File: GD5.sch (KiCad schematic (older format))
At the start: 19 parts, among them IC7 HCPL-316J, IC8 IXDD614PI, P4 CONN_01X03, P5 CONN_01X03

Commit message: uding HCPL-361J modified symbol
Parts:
- IC7: symbol HCPL-316J-RESCUE-gatedrive -> HCPL-316J
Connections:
- wire segments 41 -> 50
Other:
- moved on the sheet: IC8
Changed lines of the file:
@@
 EESchema Schematic File Version 2
-LIBS:gatedrive-rescue
 LIBS:power
 LIBS:device
@@
 LIBS:contrib
 LIBS:valves
-LIBS:GateDrive
+LIBS:74xgxx
+LIBS:ac-dc
+LIBS:actel
+LIBS:Altera
+LIBS:analog_devices
+LIBS:brooktre
+LIBS:cmos_ieee
+LIBS:dc-dc
+LIBS:diode
+LIBS:elec-unifil
+LIBS:ESD_Protection
+LIBS:ftdi
+LIBS:gennum
+LIBS:graphic
+LIBS:hc11
+LIBS:ir
+LIBS:Lattice
+LIBS:logo
+LIBS:maxim
+LIBS:microchip_dspic33dsc
+LIBS:microchip_pic10mcu
+LIBS:microchip_pic12mcu
+LIBS:microchip_pic16mcu
+LIBS:microchip_pic18mcu
+LIBS:microchip_pic32mcu
+LIBS:motor_drivers
+LIBS:msp430
+LIBS:nordicsemi
+LIBS:nxp_armmcu
+LIBS:onsemi
+LIBS:Oscillators
+LIBS:powerint
+LIBS:Power_Management
+LIBS:pspice
+LIBS:references
+LIBS:relays
+LIBS:rfcom
+LIBS:sensors
+LIBS:silabs
+LIBS:stm8
+LIBS:stm32
+LIBS:supertex
+LIBS:switches
+LIBS:transf
+LIBS:ttl_ieee
+LIBS:video
+LIBS:Worldsemi
+LIBS:Xicor
+LIBS:Zilog
 LIBS:gatedrive-cache
 EELAYER 25 0
@@
 L IXDD614PI-RESCUE-gatedrive IC8
 U 1 1 56EF642F
-P 7900 5100
-F 0 "IC8" H 7900 4900 60  0000 C CNN
-F 1 "IXDD614PI" H 7950 5450 60  0000 C CNN
-F 2 "gatedrive:DIP-8_W7.62mm_LongPads" H 7900 5200 60  0001 C CNN
-F 3 "" H 7900 5200 60  0000 C CNN
-F 4 "CHINA[already bought]" H 7900 5100 60  0001 C CNN "Supplier"
-	1    7900 5100
-	1    0    0    -1
-$EndComp
-$Comp
-L HCPL-316J-RESCUE-gatedrive IC7
+P 7950 5100
+AR Path="/56EF642F" Ref="IC8"  Part="1"
+AR Path="/56EF0563/56EF642F" Ref="IC8"  Part="1"
+F 0 "IC8" H 7950 4900 60  0000 C CNN
+F 1 "IXDD614PI" H 8000 5450 60  0000 C CNN
+F 2 "gatedrive:DIP-8_W7.62mm_LongPads" H 7950 5200 60  0001 C CNN
+F 3 "" H 7950 5200 60  0000 C CNN
+F 4 "CHINA[already bought]" H 7950 5100 60  0001 C CNN "Supplier"
+	1    7950 5100
+	1    0    0    -1
+$EndComp
+$Comp
+L HCPL-316J IC7
 U 1 1 56EF6430
-P 5550 4750
-F 0 "IC7" H 5550 4150 60  0000 C CNN
-F 1 "HCPL-316J" H 5300 5200 60  0000 C CNN
-F 2 "Housings_SOIC:SOIC-16_7.5x10.3mm_Pitch1.27mm" H 5550 4750 60  0001 C CNN
-F 3 "" H 5550 4750 60  0000 C CNN
-F 4 "CHINA [ already bought]" H 5550 4750 60  0001 C CNN "Supplier"
-	1    5550 4750
+P 5600 4850
+F 0 "IC7" H 5600 4250 60  0000 C CNN
+F 1 "HCPL-316J" H 5350 5300 60  0000 C CNN
+F 2 "Housings_SOIC:SOIC-16_7.5x10.3mm_Pitch1.27mm" H 5600 4850 60  0001 C CNN
+F 3 "" H 5600 4850 60  0000 C CNN
+F 4 "CHINA [ already bought]" H 5600 4850 60  0001 C CNN "Supplier"
+	1    5600 4850
 	1    0    0    -1
 $EndComp
@@
 Text GLabel 6450 4800 2    60   Input ~ 0
 15V5
-Text GLabel 7500 4850 0    60   Input ~ 0
-15V5
-Text GLabel 7500 5150 0    60   Input ~ 0
--5V5
-Text GLabel 8350 5150 2    60   Input ~ 0
+Text GLabel 7550 4850 0    60   Input ~ 0
+15V5
+Text GLabel 7550 5150 0    60   Input ~ 0
+-5V5
+Text GLabel 8300 5150 2    60   Input ~ 0
 -5V5
 Text GLabel 10200 4950 2    60   Input ~ 0
@@
 a cap to ensure soft turn-off, recommended by datasheet of hcpl.
 Wire Wire Line
-	6950 4950 7500 4950
-Wire Wire Line
-	6250 4950 6650 4950
-Wire Wire Line
-	6250 5050 6250 5150
-Wire Wire Line
-	6250 4750 6250 4850
+	6950 4950 7150 4950
+Wire Wire Line
+	7150 4950 7550 4950
+Wire Wire Line
+	5800 4950 6500 4950
+Wire Wire Line
+	6500 4950 6650 4950
+Wire Wire Line
+	5800 5050 6250 5100
+Wire Wire Line
+	6250 5100 5800 5150
+Wire Wire Line
+	5800 4750 6250 4800
+Wire Wire Line
+	6250 4800 5800 4850
 Connection ~ 6550 4100
 Wire Wire Line
-	6550 4650 6250 4650
+	6550 4650 5800 4650
 Wire Wire Line
 	6550 4100 6650 4100
 Wire Wire Line
-	6550 4050 6550 4650
+	6550 4050 6550 4100
+Wire Wire Line
+	6550 4100 6550 4650
 Connection ~ 8450 4950
 Wire Wire Line
@@
 Connection ~ 7150 4950
 Wire Wire Line
-	3625 4650 4850 4650
-Wire Wire Line
-	8350 4950 9050 4950
+	3625 4650 4000 4650
+Wire Wire Line
+	4000 4650 4900 4650
+Wire Wire Line
+	8300 4950 8450 4950
+Wire Wire Line
+	8450 4950 8900 4950
+Wire Wire Line
+	8900 4950 9050 4950
 Wire Wire Line
 	9350 4950 9450 4950
 Wire Wire Line
-	9750 4950 10200 4950
+	9750 4950 9950 4950
+Wire Wire Line
+	9950 4950 10200 4950
 Wire Wire Line
 	9750 5250 9950 5250
@@
 Connection ~ 9950 4950
 Wire Wire Line
-	8350 5050 8450 5050
+	8300 5050 8450 5050
 Wire Wire Line
 	8450 5050 8450 4950
@@
 	4400 4350 4400 4550
 Wire Wire Line
-	4400 4550 4850 4550
+	4400 4550 4900 4550
 Wire Wire Line
 	4000 4350 4000 4650
@@
 	4000 5300 4000 4750
 Wire Wire Line
-	4000 4750 4850 4750
-Wire Wire Line
-	4850 5150 4750 5150
+	4000 4750 4900 4750
+Wire Wire Line
+	4900 5150 4750 5150
 Wire Wire Line
 	4750 5150 4750 5300
 Wire Wire Line
-	4850 4850 4400 4850
+	4900 4850 4400 4850
 Wire Wire Line
 	4400 4850 4400 5300
 Wire Wire Line
-	6250 4450 6300 4450
+	5800 4450 6300 4450
 Wire Wire Line
 	6300 4450 6300 4350
@@
 Wire Wire Line
 	6500 5000 6500 4950
-Text GLabel 8350 4850 2    60   Input ~ 0
+Text GLabel 8300 4850 2    60   Input ~ 0
 15V5
 Text GLabel 7175 5075 3    60   Input ~ 0
 15V5
 Wire Wire Line
-	7500 5050 7175 5050
+	7550 5050 7175 5050
 Wire Wire Line
 	7175 5050 7175 5075
-Text GLabel 4850 4950 0    60   Input ~ 0
+Text GLabel 4900 4950 0    60   Input ~ 0
 ~FAULT
 Text GLabel 4750 5300 3    60   Input ~ 0
@@
 Text GLabel 1475 3050 0    60   Input ~ 0
 ~RST
-Text HLabel 4850 4450 0    60   Input ~ 0
+Text HLabel 4900 4450 0    60   Input ~ 0
 T5
 $Comp

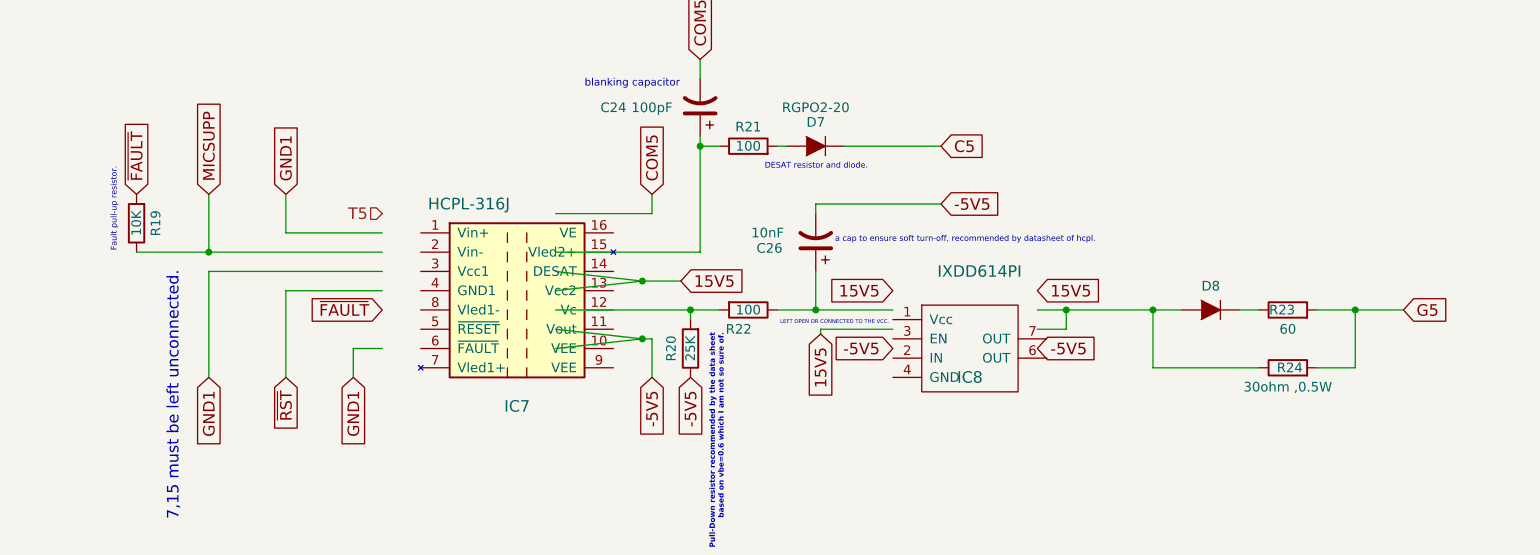
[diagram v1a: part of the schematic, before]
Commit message: cleaning the schematic
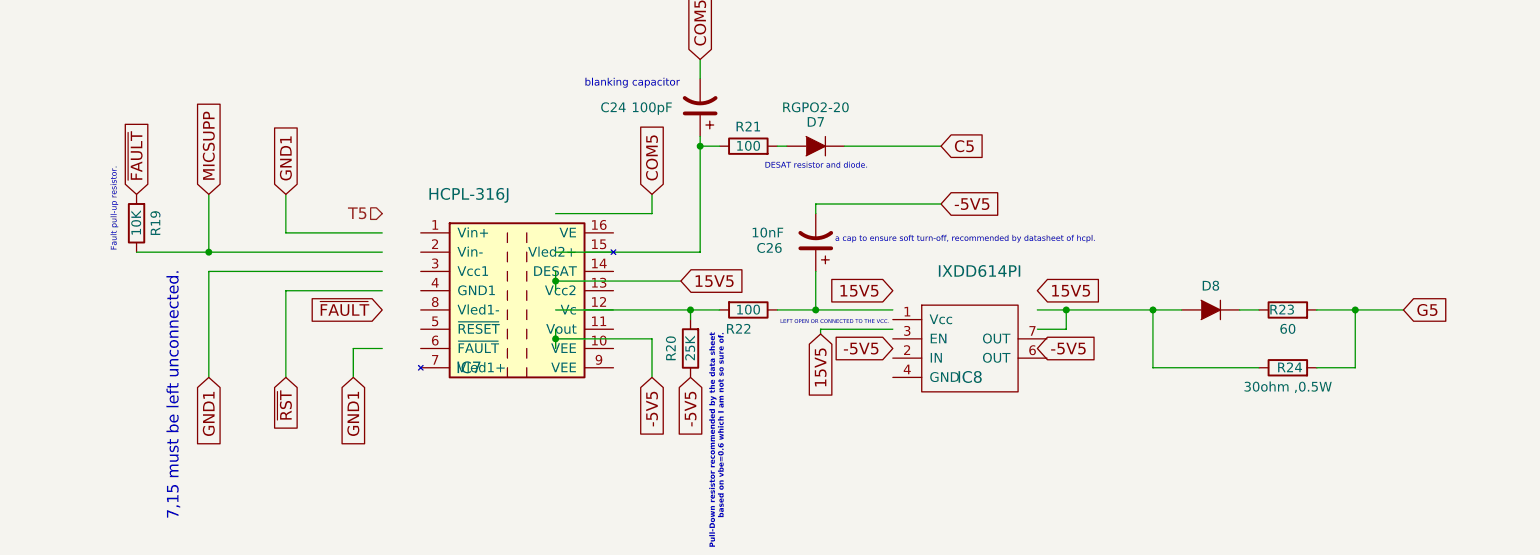
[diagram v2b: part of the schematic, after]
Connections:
- wire segments 50 -> 41
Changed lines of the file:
@@
 U 1 1 56EF6430
 P 5600 4850
-F 0 "IC7" H 5600 4250 60  0000 C CNN
-F 1 "HCPL-316J" H 5350 5300 60  0000 C CNN
+F 0 "IC7" H 5350 4450 60  0000 C CNN
+F 1 "HCPL-316J" H 5350 5350 60  0000 C CNN
 F 2 "Housings_SOIC:SOIC-16_7.5x10.3mm_Pitch1.27mm" H 5600 4850 60  0001 C CNN
 F 3 "" H 5600 4850 60  0000 C CNN
@@
 a cap to ensure soft turn-off, recommended by datasheet of hcpl.
 Wire Wire Line
-	6950 4950 7150 4950
-Wire Wire Line
-	7150 4950 7550 4950
-Wire Wire Line
-	5800 4950 6500 4950
-Wire Wire Line
-	6500 4950 6650 4950
-Wire Wire Line
-	5800 5050 6250 5100
-Wire Wire Line
-	6250 5100 5800 5150
-Wire Wire Line
-	5800 4750 6250 4800
-Wire Wire Line
-	6250 4800 5800 4850
+	6950 4950 7550 4950
+Wire Wire Line
+	5800 4950 6650 4950
+Wire Wire Line
+	5800 5050 5800 5150
+Wire Wire Line
+	5800 4750 5800 4850
 Connection ~ 6550 4100
 Wire Wire Line
@@
 	6550 4100 6650 4100
 Wire Wire Line
-	6550 4050 6550 4100
-Wire Wire Line
-	6550 4100 6550 4650
+	6550 4050 6550 4650
 Connection ~ 8450 4950
 Wire Wire Line
@@
 Connection ~ 7150 4950
 Wire Wire Line
-	3625 4650 4000 4650
-Wire Wire Line
-	4000 4650 4900 4650
-Wire Wire Line
-	8300 4950 8450 4950
-Wire Wire Line
-	8450 4950 8900 4950
-Wire Wire Line
-	8900 4950 9050 4950
+	3625 4650 4900 4650
+Wire Wire Line
+	8300 4950 9050 4950
 Wire Wire Line
 	9350 4950 9450 4950
 Wire Wire Line
-	9750 4950 9950 4950
-Wire Wire Line
-	9950 4950 10200 4950
+	9750 4950 10200 4950
 Wire Wire Line
 	9750 5250 9950 5250
@@
 	6300 5300 6300 5100
 Wire Wire Line
-	6300 5100 6250 5100
-Connection ~ 6250 5100
-Wire Wire Line
-	6250 4800 6450 4800
-Connection ~ 6250 4800
+	6300 5100 5800 5100
+Connection ~ 5800 5100
+Wire Wire Line
+	5800 4800 6450 4800
+Connection ~ 5800 4800
 Wire Wire Line
 	8900 5250 9450 5250

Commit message: completion of the layout, initial layout of the protection circuit, reducing number of circuit to 7
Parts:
- C22, C23, C24, C26, C27, C28: footprint Capacitors_ThroughHole:C_Disc_D3_P2.5 -> gatedrive:C_Disc
- D7: footprint Diodes_ThroughHole:Diode_DO-201AD_Horizontal_RM15 -> Diodes_ThroughHole:Diode_DO-41_SOD81_Horizontal_RM10
- R19: footprint Resistors_ThroughHole:Resistor_Vertical_RM5mm -> Resistors_ThroughHole:Resistor_Horizontal_RM10mm
- R23, R24: footprint Resistors_ThroughHole:Resistor_Horizontal_RM20mm -> gatedrive:Resistor_multi
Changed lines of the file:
@@
 EESchema Schematic File Version 2
+LIBS:Symbols_DCDC-ACDC-Converter_RevC_20Jul2012
+LIBS:Symbols_EN60617_13Mar2013
+LIBS:Symbols_EN60617-10_HF-Radio_DRAFT_12Sep2013
+LIBS:Symbols_ICs-Diskrete_RevD10
+LIBS:Symbols_ICs-Opto_RevB_16Sep2013
+LIBS:Symbols_Microcontroller_Philips-NXP_RevA_06Oct2013
+LIBS:SymbolsSimilarEN60617+oldDIN617-RevE8
+LIBS:Symbols_Socket-DIN41612_RevA
+LIBS:Symbols_Transformer-Diskrete_RevA
 LIBS:power
 LIBS:device
@@
 $Descr A4 11693 8268
 encoding utf-8
-Sheet 5 10
+Sheet 5 9
 Title "IGBT GATE DRIVE SCHEMATIC."
 Date "2016-03-02"
@@
 F 0 "D7" H 7150 3976 50  0000 C CNN
 F 1 "RGPO2-20" H 7150 3900 50  0000 C CNN
-F 2 "Diodes_ThroughHole:Diode_DO-201AD_Horizontal_RM15" H 7150 4100 50  0001 C CNN
+F 2 "Diodes_ThroughHole:Diode_DO-41_SOD81_Horizontal_RM10" H 7150 4100 50  0001 C CNN
 F 3 "" H 7150 4100 50  0000 C CNN
 F 4 "El-Amir" H 7150 4100 60  0001 C CNN "Supplier"
@@
 F 0 "R19" V 3525 4500 50  0000 C CNN
 F 1 "10K" V 3625 4500 50  0000 C CNN
-F 2 "Resistors_ThroughHole:Resistor_Vertical_RM5mm" V 3555 4500 50  0001 C CNN
+F 2 "Resistors_ThroughHole:Resistor_Horizontal_RM10mm" V 3555 4500 50  0001 C CNN
 F 3 "" H 3625 4500 50  0000 C CNN
 F 4 "EL AMIR" H 3625 4500 60  0001 C CNN "Supplier"
@@
 F 0 "C22" H 4150 2150 50  0000 C CNN
 F 1 "0.1uF" H 4250 2050 50  0000 C CNN
-F 2 "Capacitors_ThroughHole:C_Disc_D3_P2.5" H 4488 2000 50  0001 C CNN
+F 2 "gatedrive:C_Disc" H 4488 2000 50  0001 C CNN
 F 3 "" H 4450 2150 50  0000 C CNN
 F 4 "EL AMIR" H 4450 2150 60  0001 C CNN "Supplier"
@@
 F 0 "C24" H 7000 3900 50  0000 C CNN
 F 1 "100pF" H 6800 3900 50  0000 C CNN
-F 2 "Capacitors_ThroughHole:C_Disc_D3_P2.5" H 6588 3750 50  0001 C CNN
+F 2 "gatedrive:C_Disc" H 6588 3750 50  0001 C CNN
 F 3 "" H 6550 3900 50  0000 C CNN
 	1    6550 3900
@@
 F 0 "C28" H 8450 2150 50  0000 C CNN
 F 1 "0.1uF" H 8450 2050 50  0000 C CNN
-F 2 "Capacitors_ThroughHole:C_Disc_D3_P2.5" H 8888 2000 50  0001 C CNN
+F 2 "gatedrive:C_Disc" H 8888 2000 50  0001 C CNN
 F 3 "" H 8850 2150 50  0000 C CNN
 	1    8850 2150
@@
 F 0 "C27" H 7400 2150 50  0000 C CNN
 F 1 "0.1uF" H 7400 2050 50  0000 C CNN
-F 2 "Capacitors_ThroughHole:C_Disc_D3_P2.5" H 7788 2000 50  0001 C CNN
+F 2 "gatedrive:C_Disc" H 7788 2000 50  0001 C CNN
 F 3 "" H 7750 2150 50  0000 C CNN
 	1    7750 2150
@@
 F 0 "C23" H 5150 2150 50  0000 C CNN
 F 1 "0.1uF" H 5150 2050 50  0000 C CNN
-F 2 "Capacitors_ThroughHole:C_Disc_D3_P2.5" H 5538 2000 50  0001 C CNN
+F 2 "gatedrive:C_Disc" H 5538 2000 50  0001 C CNN
 F 3 "" H 5500 2150 50  0000 C CNN
 	1    5500 2150
@@
 LEFT OPEN OR CONNECTED TO THE VCC.
 $Comp
-L PWR_FLAG #FLG022
+L PWR_FLAG #FLG015
 U 1 1 56EF643D
 P 1300 3800
-F 0 "#FLG022" H 1300 3895 50  0001 C CNN
+F 0 "#FLG015" H 1300 3895 50  0001 C CNN
 F 1 "PWR_FLAG" H 1300 4024 50  0000 C CNN
 F 2 "" H 1300 3800 50  0000 C CNN
@@
 $EndComp
 $Comp
-L PWR_FLAG #FLG023
+L PWR_FLAG #FLG016
 U 1 1 56EF643E
 P 1750 3800
-F 0 "#FLG023" H 1750 3895 50  0001 C CNN
+F 0 "#FLG016" H 1750 3895 50  0001 C CNN
 F 1 "PWR_FLAG" H 1750 4024 50  0000 C CNN
 F 2 "" H 1750 3800 50  0000 C CNN
@@
 $EndComp
 $Comp
-L PWR_FLAG #FLG024
+L PWR_FLAG #FLG017
 U 1 1 56EF643F
 P 1750 2650
-F 0 "#FLG024" H 1750 2745 50  0001 C CNN
+F 0 "#FLG017" H 1750 2745 50  0001 C CNN
 F 1 "PWR_FLAG" H 1750 2874 50  0000 C CNN
 F 2 "" H 1750 2650 50  0000 C CNN
@@
 $EndComp
 $Comp
-L PWR_FLAG #FLG025
+L PWR_FLAG #FLG018
 U 1 1 56EF6440
 P 900 2650
-F 0 "#FLG025" H 900 2745 50  0001 C CNN
+F 0 "#FLG018" H 900 2745 50  0001 C CNN
 F 1 "PWR_FLAG" H 900 2874 50  0000 C CNN
 F 2 "" H 900 2650 50  0000 C CNN
@@
 $EndComp
 $Comp
-L PWR_FLAG #FLG026
+L PWR_FLAG #FLG019
 U 1 1 56EF6441
 P 1300 2650
-F 0 "#FLG026" H 1300 2745 50  0001 C CNN
+F 0 "#FLG019" H 1300 2745 50  0001 C CNN
 F 1 "PWR_FLAG" H 1300 2874 50  0000 C CNN
 F 2 "" H 1300 2650 50  0000 C CNN
@@
 $EndComp
 $Comp
-L PWR_FLAG #FLG027
+L PWR_FLAG #FLG020
 U 1 1 56EF6442
 P 900 3800
-F 0 "#FLG027" H 900 3895 50  0001 C CNN
+F 0 "#FLG020" H 900 3895 50  0001 C CNN
 F 1 "PWR_FLAG" H 900 4024 50  0000 C CNN
 F 2 "" H 900 3800 50  0000 C CNN
@@
 F 0 "C26" H 7390 4630 50  0000 C CNN
 F 1 "10nF" H 7400 4550 50  0000 C CNN
-F 2 "Capacitors_ThroughHole:C_Disc_D3_P2.5" H 7188 4450 50  0001 C CNN
+F 2 "gatedrive:C_Disc" H 7188 4450 50  0001 C CNN
 F 3 "" H 7150 4600 50  0000 C CNN
 	1    7150 4600
@@
 F 0 "R23" V 9600 4980 50  0000 C CNN
 F 1 "60" V 9500 4950 50  0000 C CNN
-F 2 "Resistors_ThroughHole:Resistor_Horizontal_RM20mm" V 9530 4950 50  0001 C CNN
+F 2 "gatedrive:Resistor_multi" V 9530 4950 50  0001 C CNN
 F 3 "" H 9600 4950 50  0000 C CNN
 F 4 "Al amir" H 9600 4950 60  0001 C CNN "Supplier"
@@
 F 0 "R24" V 9600 5240 50  0000 C CNN
 F 1 "30ohm ,0.5W" V 9500 5250 50  0000 C CNN
-F 2 "Resistors_ThroughHole:Resistor_Horizontal_RM20mm" V 9530 5250 50  0001 C CNN
+F 2 "gatedrive:Resistor_multi" V 9530 5250 50  0001 C CNN
 F 3 "" H 9600 5250 50  0000 C CNN
 F 4 "Supplier_name" H 9600 5250 60  0001 C CNN "Supplier"
@@
 	6950 4100 7000 4100
 $Comp
-L PWR_FLAG #FLG028
+L PWR_FLAG #FLG021
 U 1 1 56EF6449
 P 1475 3050
-F 0 "#FLG028" H 1475 3145 50  0001 C CNN
+F 0 "#FLG021" H 1475 3145 50  0001 C CNN
 F 1 "PWR_FLAG" V 1625 3050 50  0000 C CNN
 F 2 "" H 1475 3050 50  0000 C CNN

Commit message: yet another enhancements .
the protection section still is incomplete.
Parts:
- IC8: symbol IXDD614PI-RESCUE-gatedrive -> IXDD614PI
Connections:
- wire segments 41 -> 50
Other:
- moved on the sheet: IC7
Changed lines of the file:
@@
 $Descr A4 11693 8268
 encoding utf-8
-Sheet 5 9
+Sheet 4 9
 Title "IGBT GATE DRIVE SCHEMATIC."
 Date "2016-03-02"
@@
 $EndDescr
 $Comp
-L IXDD614PI-RESCUE-gatedrive IC8
+L IXDD614PI IC8
 U 1 1 56EF642F
-P 7950 5100
+P 7950 5050
 AR Path="/56EF642F" Ref="IC8"  Part="1"
 AR Path="/56EF0563/56EF642F" Ref="IC8"  Part="1"
-F 0 "IC8" H 7950 4900 60  0000 C CNN
-F 1 "IXDD614PI" H 8000 5450 60  0000 C CNN
-F 2 "gatedrive:DIP-8_W7.62mm_LongPads" H 7950 5200 60  0001 C CNN
-F 3 "" H 7950 5200 60  0000 C CNN
-F 4 "CHINA[already bought]" H 7950 5100 60  0001 C CNN "Supplier"
-	1    7950 5100
+F 0 "IC8" H 7950 4850 60  0000 C CNN
+F 1 "IXDD614PI" H 8000 5400 60  0000 C CNN
+F 2 "gatedrive:DIP-8_W7.62mm_LongPads" H 7950 5150 60  0001 C CNN
+F 3 "" H 7950 5150 60  0000 C CNN
+F 4 "CHINA[already bought]" H 7950 5050 60  0001 C CNN "Supplier"
+	1    7950 5050
 	1    0    0    -1
 $EndComp
@@
 L HCPL-316J IC7
 U 1 1 56EF6430
-P 5600 4850
-F 0 "IC7" H 5350 4450 60  0000 C CNN
-F 1 "HCPL-316J" H 5350 5350 60  0000 C CNN
-F 2 "Housings_SOIC:SOIC-16_7.5x10.3mm_Pitch1.27mm" H 5600 4850 60  0001 C CNN
-F 3 "" H 5600 4850 60  0000 C CNN
-F 4 "CHINA [ already bought]" H 5600 4850 60  0001 C CNN "Supplier"
-	1    5600 4850
+P 5300 4750
+AR Path="/56EF6430" Ref="IC7"  Part="1"
+AR Path="/56EF0563/56EF6430" Ref="IC7"  Part="1"
+F 0 "IC7" H 5050 4350 60  0000 C CNN
+F 1 "HCPL-316J" H 5050 5250 60  0000 C CNN
+F 2 "Housings_SOIC:SOIC-16_7.5x10.3mm_Pitch1.27mm" H 5300 4750 60  0001 C CNN
+F 3 "" H 5300 4750 60  0000 C CNN
+F 4 "CHINA [ already bought]" H 5300 4750 60  0001 C CNN "Supplier"
+	1    5300 4750
 	1    0    0    -1
 $EndComp
@@
 Text GLabel 7550 5150 0    60   Input ~ 0
 -5V5
-Text GLabel 8300 5150 2    60   Input ~ 0
+Text GLabel 8350 5150 2    60   Input ~ 0
 -5V5
 Text GLabel 10200 4950 2    60   Input ~ 0
@@
 a cap to ensure soft turn-off, recommended by datasheet of hcpl.
 Wire Wire Line
-	6950 4950 7550 4950
-Wire Wire Line
-	5800 4950 6650 4950
-Wire Wire Line
-	5800 5050 5800 5150
-Wire Wire Line
-	5800 4750 5800 4850
+	6950 4950 7150 4950
+Wire Wire Line
+	7150 4950 7550 4950
+Wire Wire Line
+	5800 4950 6500 4950
+Wire Wire Line
+	6500 4950 6650 4950
+Wire Wire Line
+	5800 5050 5800 5100
+Wire Wire Line
+	5800 5100 5800 5150
+Wire Wire Line
+	5800 4750 5800 4800
+Wire Wire Line
+	5800 4800 5800 4850
 Connection ~ 6550 4100
 Wire Wire Line
@@
 	6550 4100 6650 4100
 Wire Wire Line
-	6550 4050 6550 4650
+	6550 4050 6550 4100
+Wire Wire Line
+	6550 4100 6550 4650
 Connection ~ 8450 4950
 Wire Wire Line
@@
 Connection ~ 7150 4950
 Wire Wire Line
-	3625 4650 4900 4650
-Wire Wire Line
-	8300 4950 9050 4950
+	3625 4650 4000 4650
+Wire Wire Line
+	4000 4650 4800 4650
+Wire Wire Line
+	8350 4950 8450 4950
+Wire Wire Line
+	8450 4950 8900 4950
+Wire Wire Line
+	8900 4950 9050 4950
 Wire Wire Line
 	9350 4950 9450 4950
 Wire Wire Line
-	9750 4950 10200 4950
+	9750 4950 9950 4950
+Wire Wire Line
+	9950 4950 10200 4950
 Wire Wire Line
 	9750 5250 9950 5250
@@
 Connection ~ 9950 4950
 Wire Wire Line
-	8300 5050 8450 5050
+	8350 5050 8450 5050
 Wire Wire Line
 	8450 5050 8450 4950
@@
 	4400 4350 4400 4550
 Wire Wire Line
-	4400 4550 4900 4550
+	4400 4550 4800 4550
 Wire Wire Line
 	4000 4350 4000 4650
@@
 	4000 5300 4000 4750
 Wire Wire Line
-	4000 4750 4900 4750
-Wire Wire Line
-	4900 5150 4750 5150
+	4000 4750 4800 4750
+Wire Wire Line
+	4800 5150 4750 5150
 Wire Wire Line
 	4750 5150 4750 5300
 Wire Wire Line
-	4900 4850 4400 4850
+	4800 4850 4400 4850
 Wire Wire Line
 	4400 4850 4400 5300
@@
 Wire Wire Line
 	7175 5050 7175 5075
-Text GLabel 4900 4950 0    60   Input ~ 0
+Text GLabel 4800 4950 0    60   Input ~ 0
 ~FAULT
 Text GLabel 4750 5300 3    60   Input ~ 0
@@
 Text GLabel 1475 3050 0    60   Input ~ 0
 ~RST
-Text HLabel 4900 4450 0    60   Input ~ 0
+Text HLabel 4800 4450 0    60   Input ~ 0
 T5
 $Comp
